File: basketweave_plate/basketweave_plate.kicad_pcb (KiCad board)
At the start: 2 copper layers, 371.5 x 119.1 mm, 1 part

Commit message: Move macro keys to the right and encoder to the left
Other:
- outline, holes or cut-outs redrawn

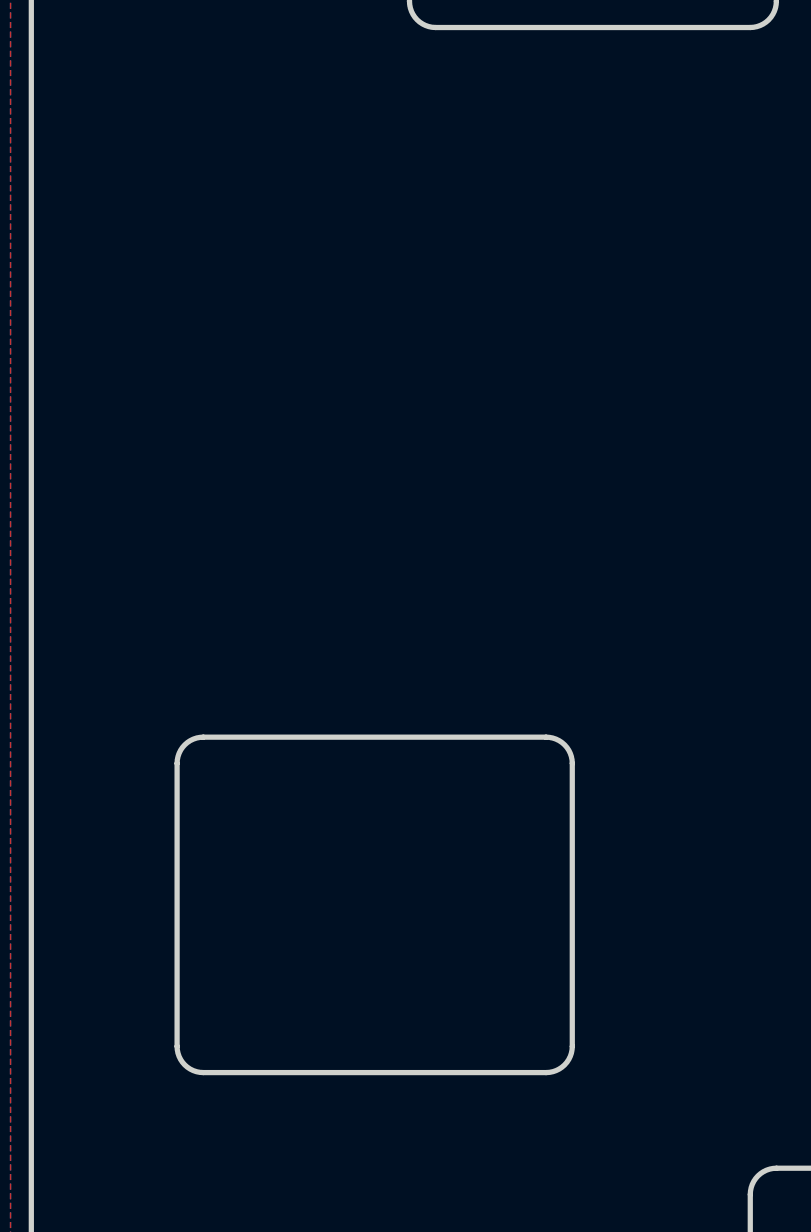
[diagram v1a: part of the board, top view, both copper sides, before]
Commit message: Make macro keys symmetric on both sides; move encoder to the left
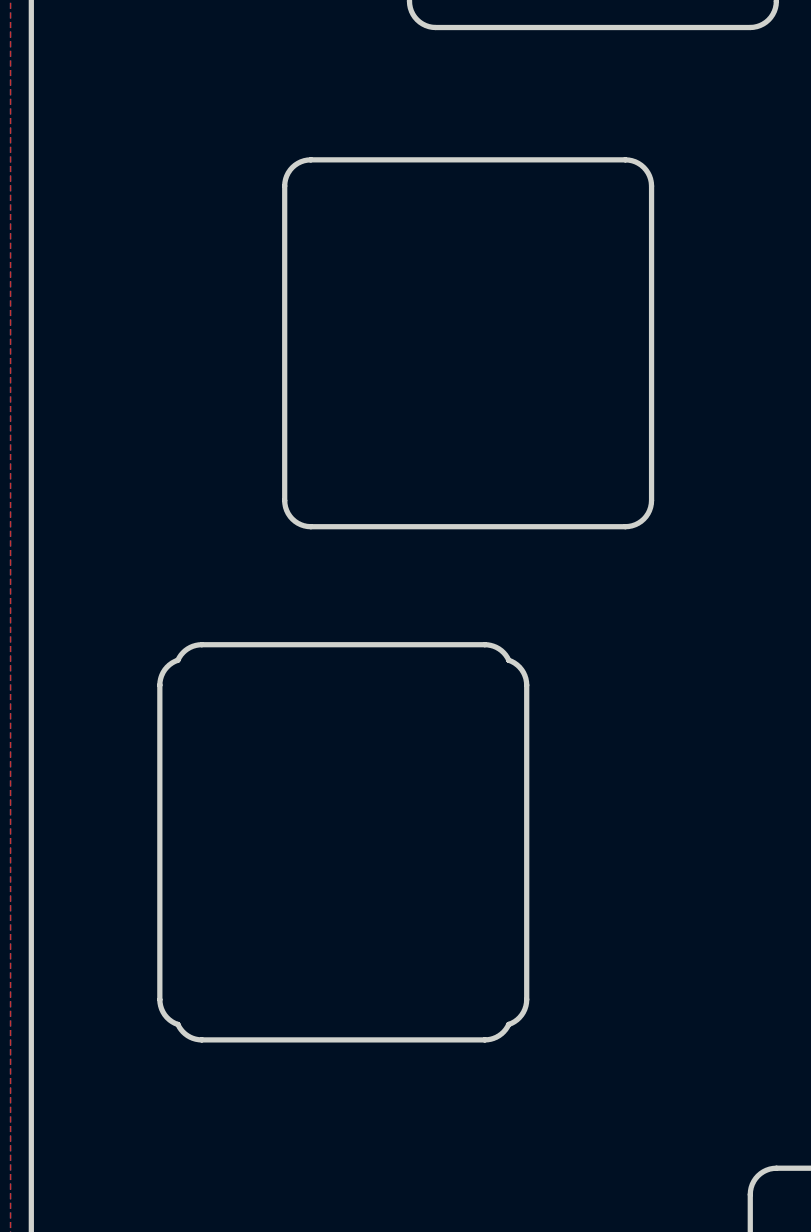
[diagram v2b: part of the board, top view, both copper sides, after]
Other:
- outline, holes or cut-outs redrawn
